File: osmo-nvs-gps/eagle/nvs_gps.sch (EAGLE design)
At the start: 20 parts, among them K1 JACK2.5_SJ-2523, K2 JACK2.5_SJ-2523, U1 NV08C-CSM, X1 MOLEX_MCX_V

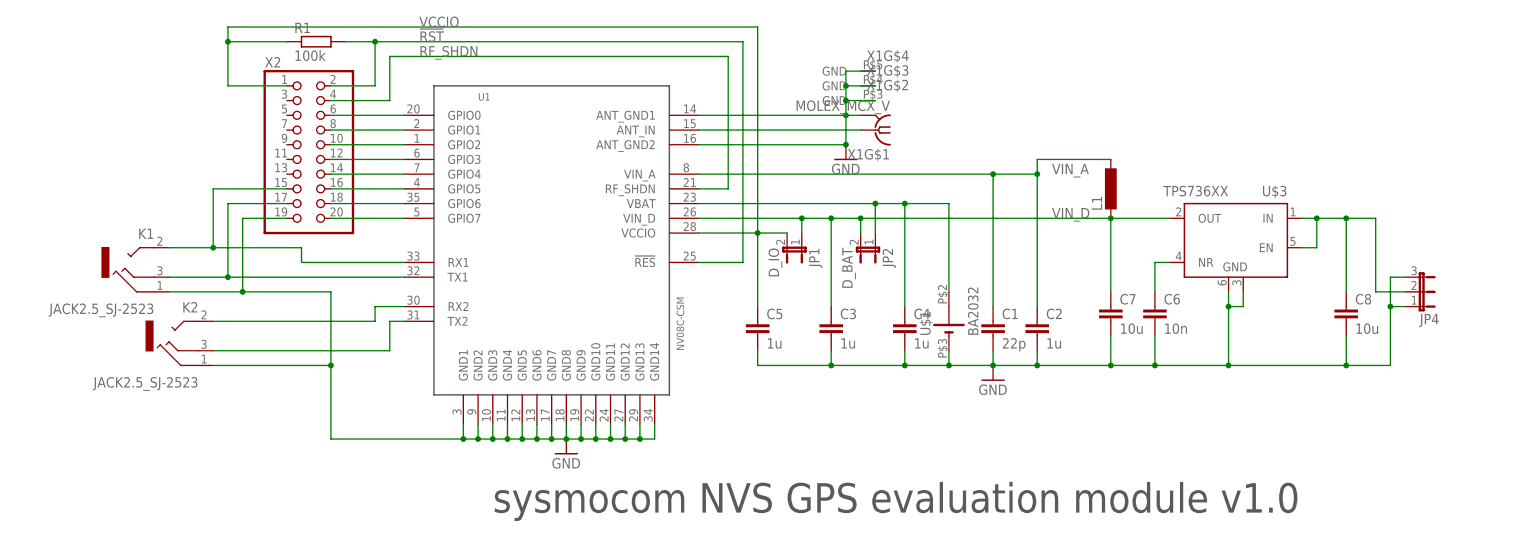
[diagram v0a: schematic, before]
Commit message: add a power-indicator LED to the NVS board and tag it v2
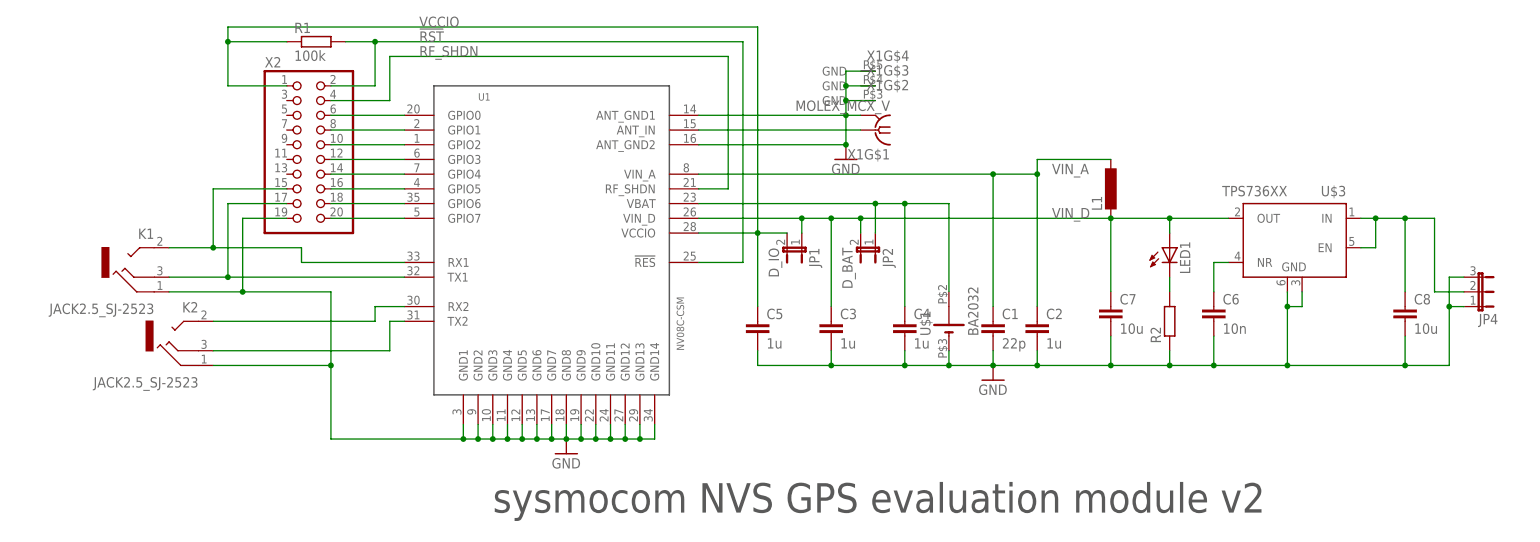
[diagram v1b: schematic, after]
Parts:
- added LED1: (no value), SparkFun-LED:LED0603
- added R2: (no value), rcl:R-EU_R0603
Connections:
- new net N$14: LED1.C, R2.2
- net GND: now also R2.1
- net VIN_D: now also LED1.A
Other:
- note added: "sysmocom NVS GPS evaluation module v2"
- note removed: "sysmocom NVS GPS evaluation module v1.0"
- moved on the sheet: C6, C8, JP4, U$3

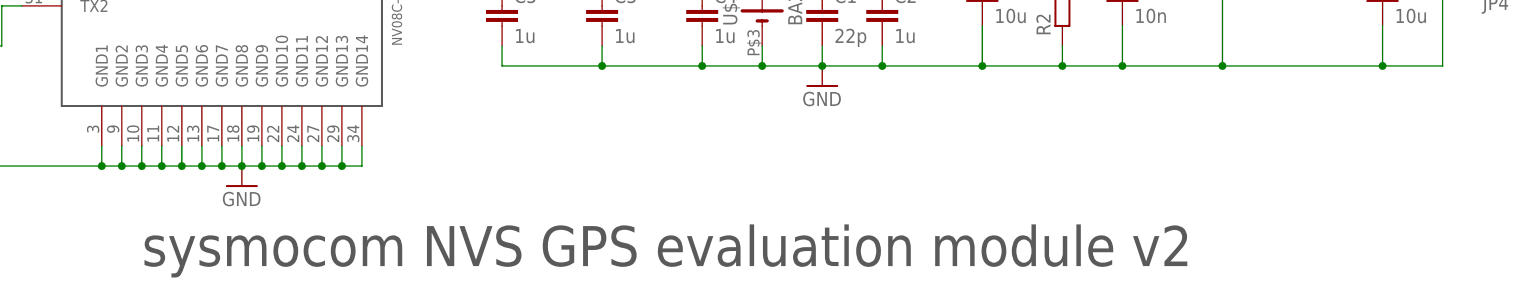
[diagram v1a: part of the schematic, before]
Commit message: avoid short-circuit of power LED
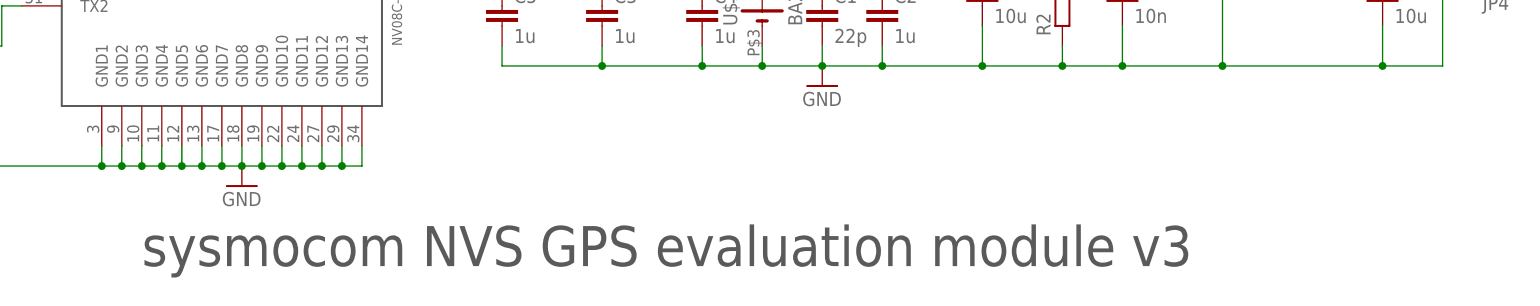
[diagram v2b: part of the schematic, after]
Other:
- note added: "sysmocom NVS GPS evaluation module v3"
- note removed: "sysmocom NVS GPS evaluation module v2"
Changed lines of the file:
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@@
 <?xml version="1.0" encoding="utf-8"?>
 <!DOCTYPE eagle SYSTEM "eagle.dtd">
-<eagle version="6.0">
+<eagle version="6.4">
 <drawing>
 <settings>
@@
 <sheet>
 <plain>
-<text x="55.88" y="12.7" size="5.08" layer="97">sysmocom NVS GPS evaluation module v2</text>
+<text x="55.88" y="12.7" size="5.08" layer="97">sysmocom NVS GPS evaluation module v3</text>
 </plain>
 <instances>
